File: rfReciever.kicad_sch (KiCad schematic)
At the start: 38 parts, among them J1 1054440001, SW1 RF_RESET, SW2 RF_SLEEP, U1 CP2102N-Axx-xQFN20, U2 USBLC6-2SC6, X1 DigiXBeeRX900Micro

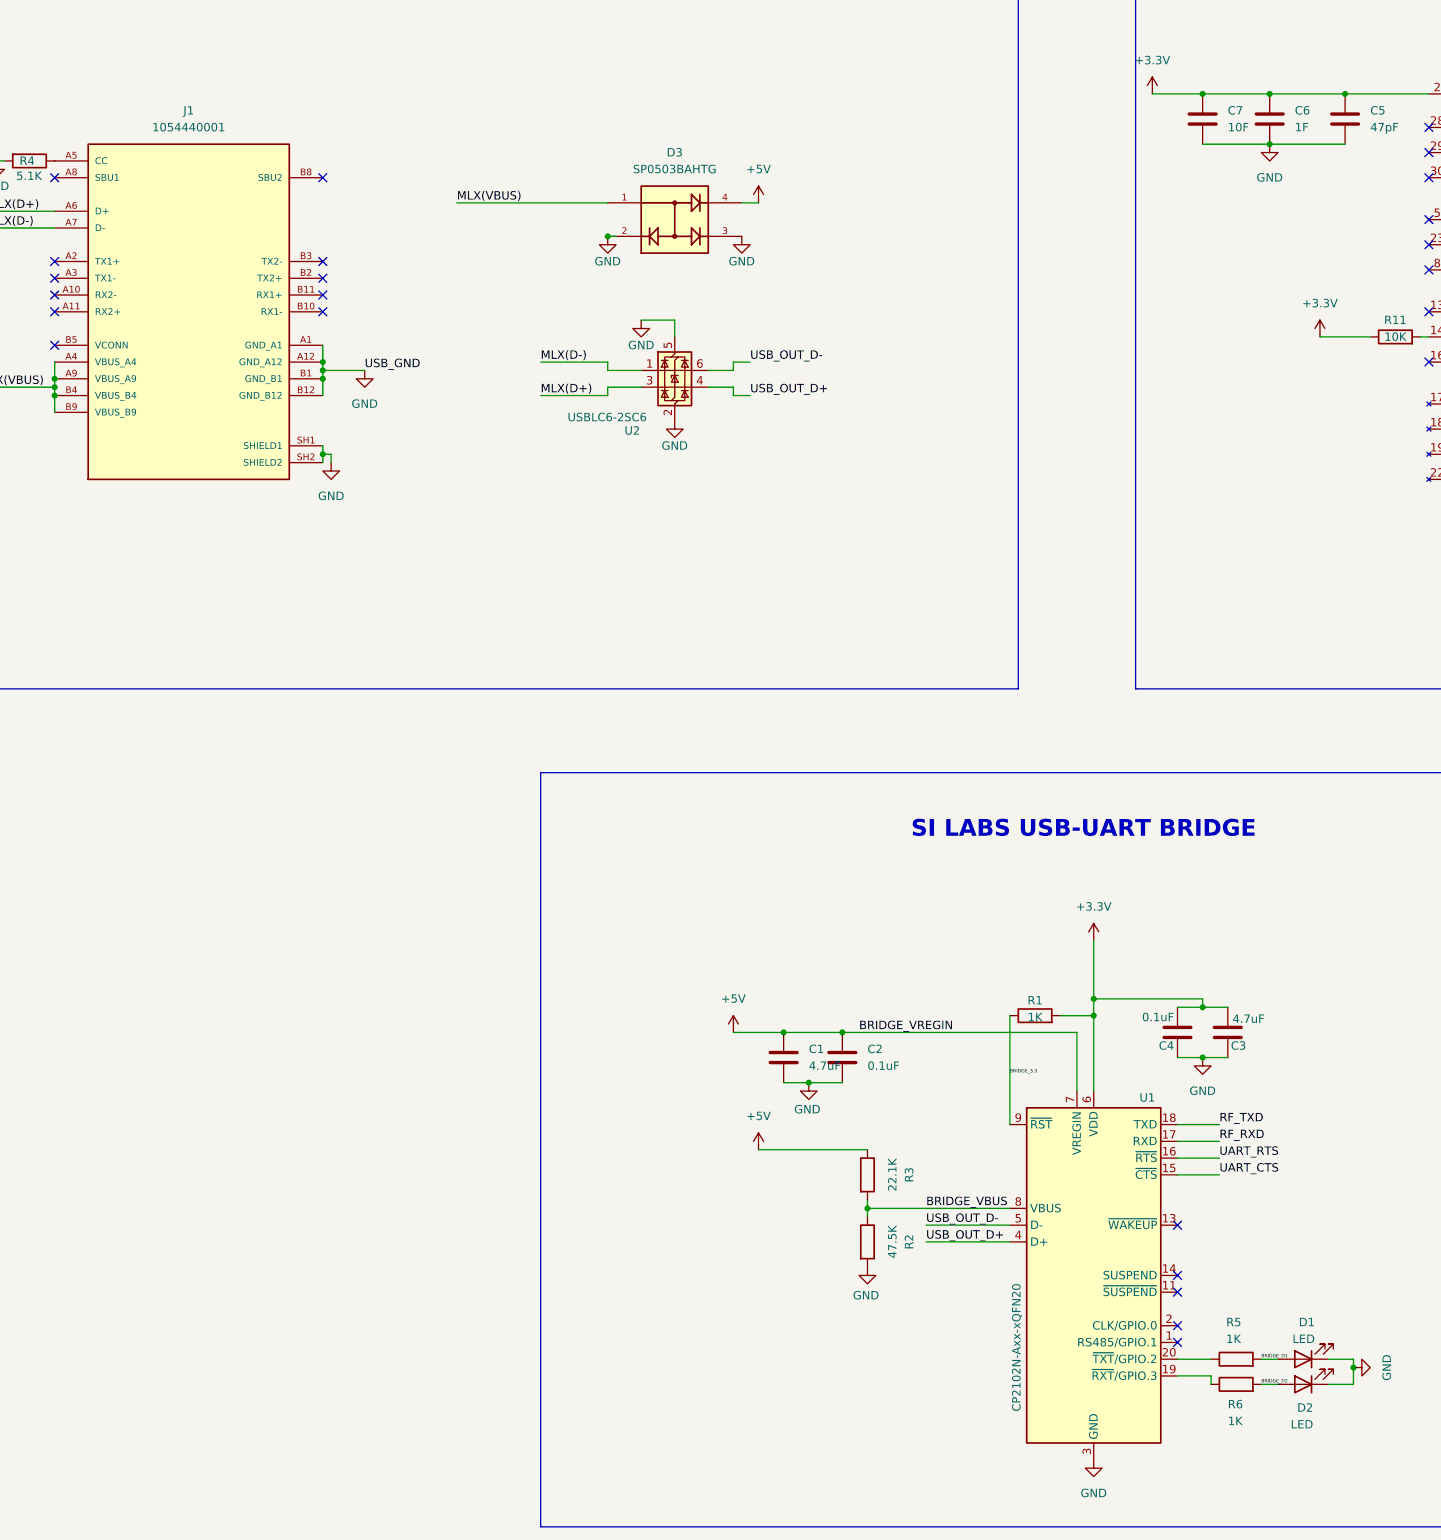
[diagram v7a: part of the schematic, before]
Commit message: BOM with mouser part #
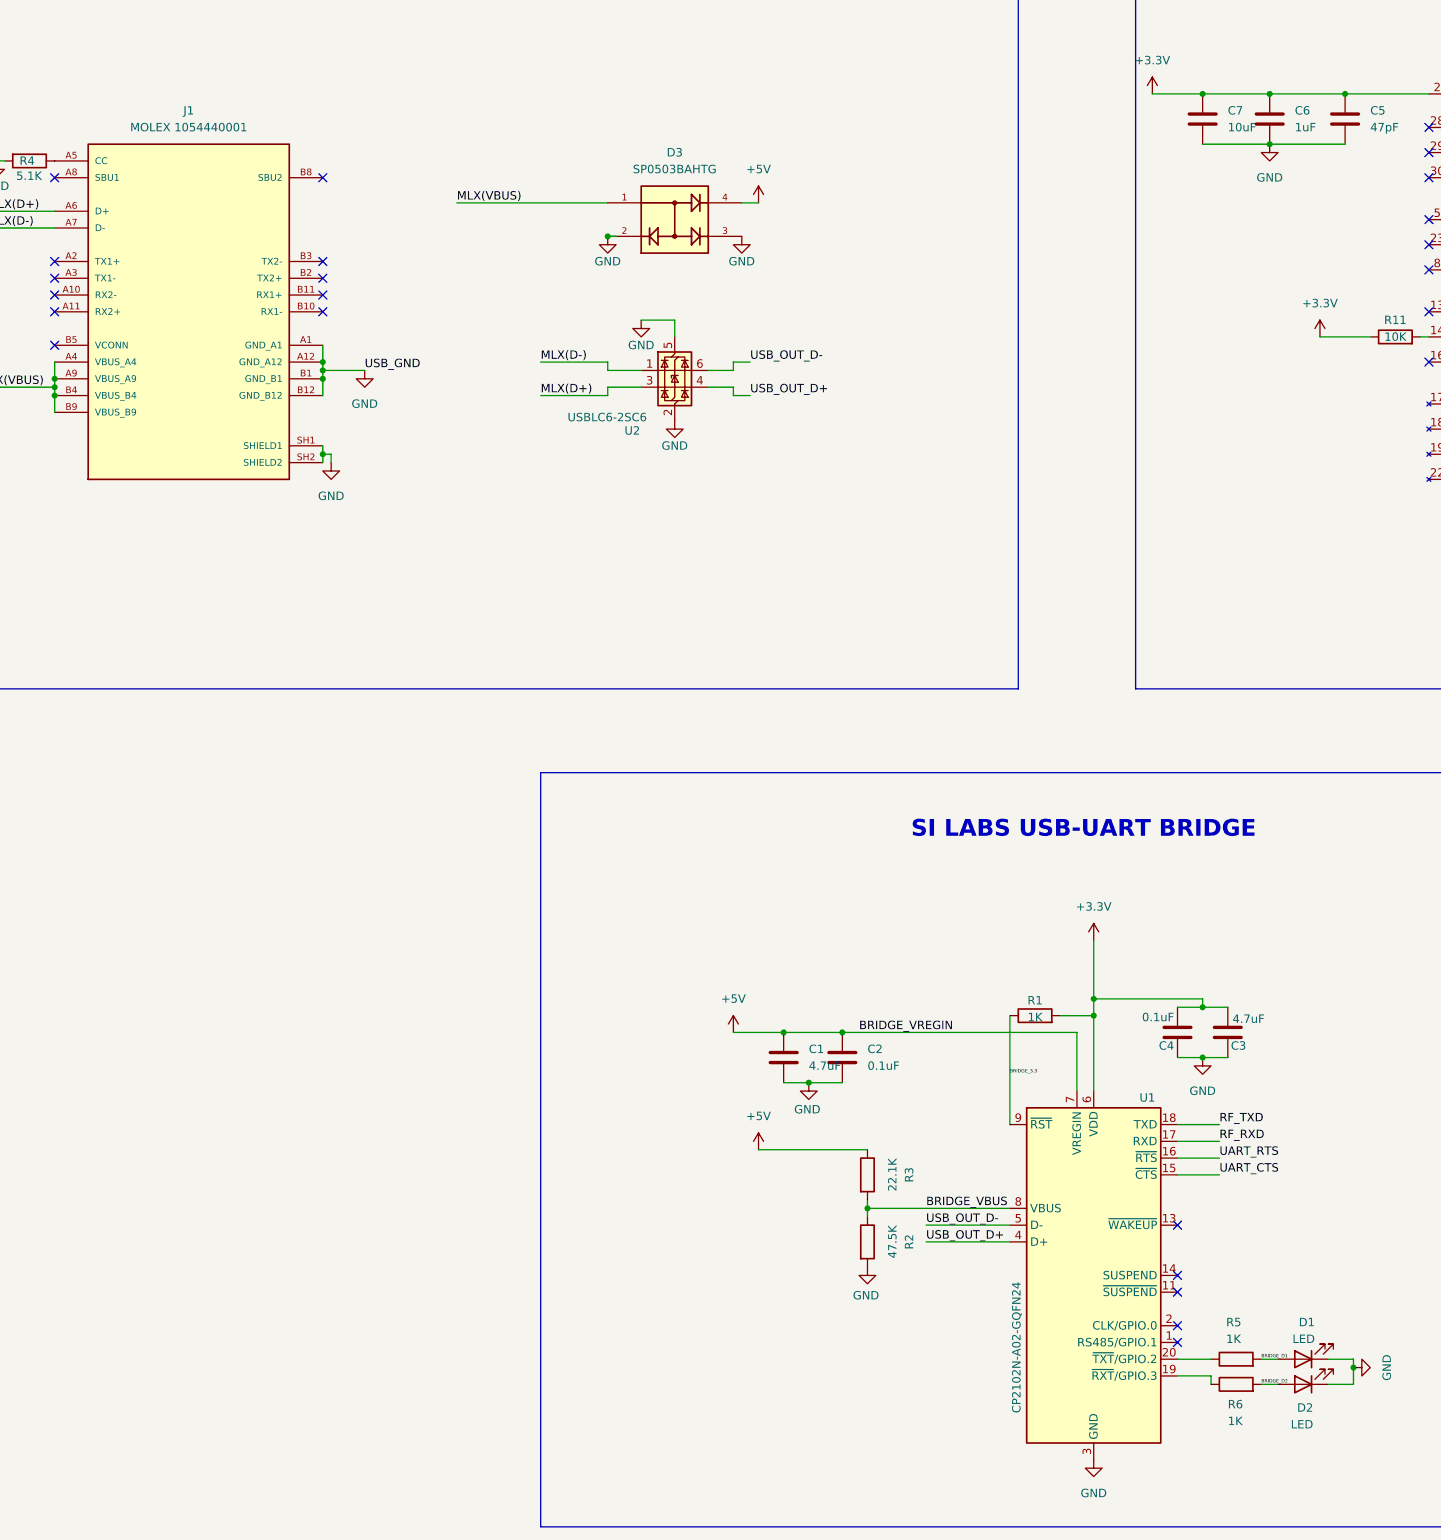
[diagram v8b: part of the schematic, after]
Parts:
- C6: value 1F -> 1uF
- C7: value 10F -> 10uF
- J1: value 1054440001 -> MOLEX 1054440001
- U1: value CP2102N-Axx-xQFN20 -> CP2102N-A02-GQFN24
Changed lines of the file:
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@@
 			)
 		)
-		(property "Value" "1F"
+		(property "Value" "1uF"
 			(at 227.33 59.6899 0)
 			(effects
@@
 			)
 		)
-		(property "Datasheet" ""
+		(property "Datasheet" "https://www.littelfuse.com/assetdocs/tvs-diode-array-spasp050xba-lead-freegreen-datasheet?assetguid=15a03de1-f0c6-457a-95f1-55d449fdd756"
 			(at 133.35 73.66 0)
 			(effects
@@
 			)
 		)
-		(property "Value" "10F"
+		(property "Value" "10uF"
 			(at 217.17 59.6899 0)
 			(effects
@@
 			)
 		)
-		(property "Value" "CP2102N-Axx-xQFN20"
+		(property "Value" "CP2102N-A02-GQFN24"
 			(at 185.166 244.602 90)
 			(effects
@@
 			)
 		)
-		(property "Datasheet" "https://www.silabs.com/documents/public/data-sheets/cp2102n-datasheet.pdf"
+		(property "Datasheet" "https://datasheet.octopart.com/CP2102N-A02-GQFN24-Silicon-Labs-datasheet-138898368.pdf"
 			(at 198.12 252.73 0)
 			(effects
@@
 			)
 		)
-		(property "Value" "1054440001"
+		(property "Value" "MOLEX 1054440001"
 			(at 59.69 59.69 0)
 			(effects
@@
 			)
 		)
-		(property "Datasheet" ""
+		(property "Datasheet" "https://www.molex.com/en-us/products/part-detail-pdf/1054440001?display=pdf"
 			(at 59.69 87.63 0)
 			(effects
